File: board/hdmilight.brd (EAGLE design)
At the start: 68.5 x 68.6 mm, 72 parts, among them IC1 REG1117, IC2 REG1117, Q1 28.6363MHz

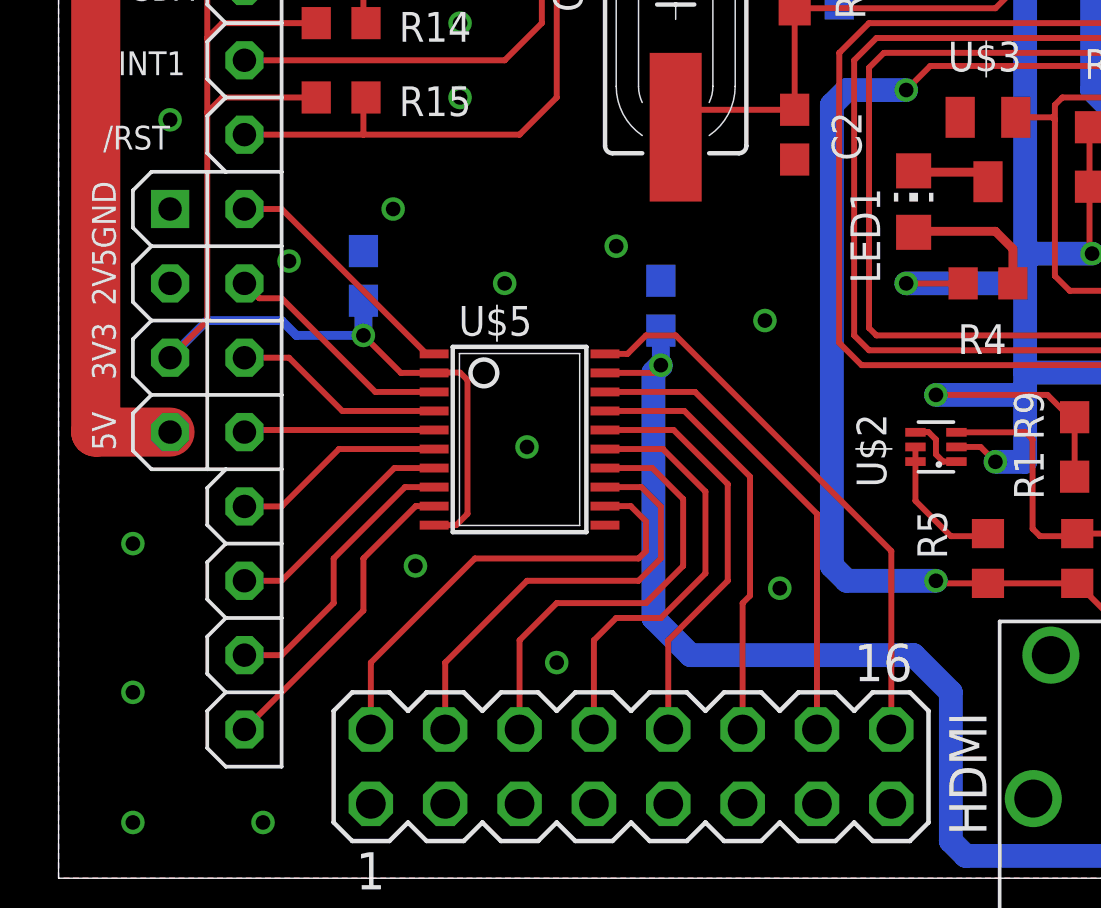
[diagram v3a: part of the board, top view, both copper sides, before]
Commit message: receiver board: replaced TXB0108 level shifter with a 74HCT541
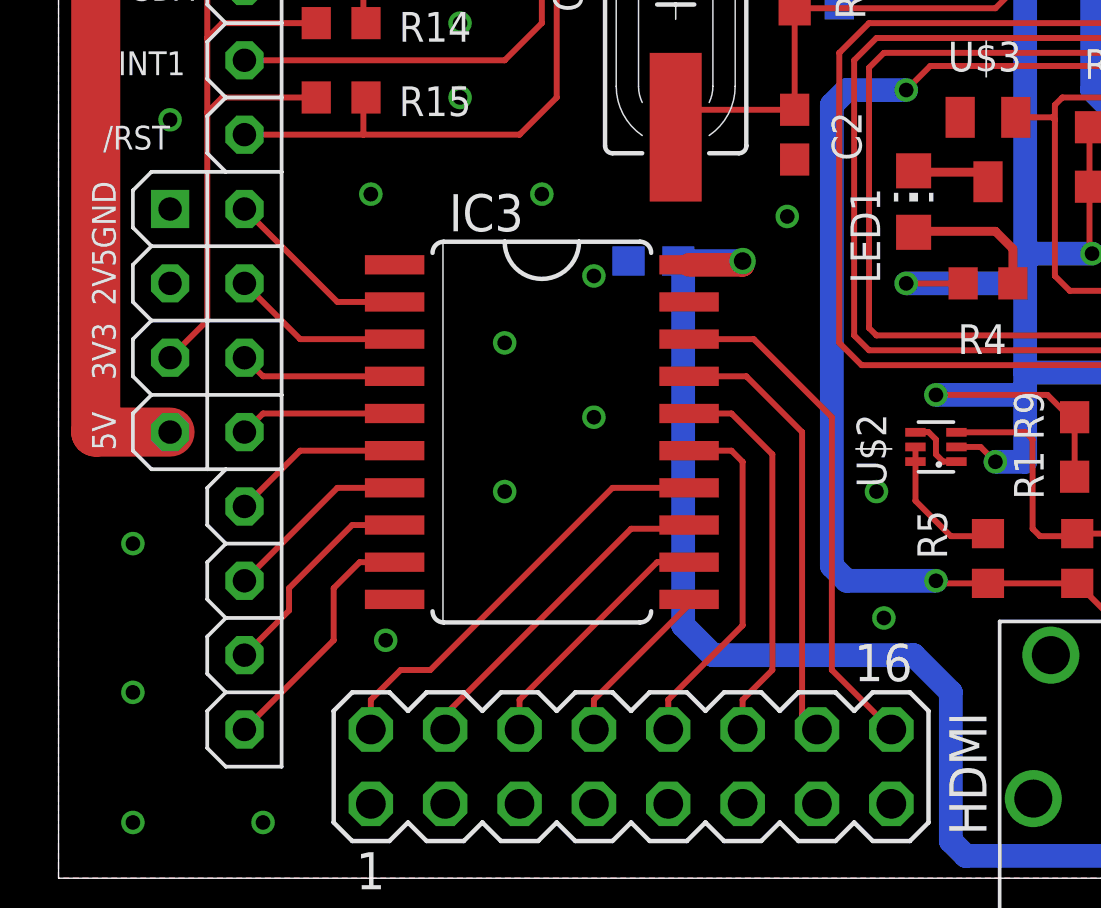
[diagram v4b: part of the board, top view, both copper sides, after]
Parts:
- removed C20: 0.1uF, resistor:C0603
- removed U$5: TXB0108, __SR:TSSOP20
- added IC3: 74HCT541DW, 74xx-eu:SO20W
- moved C21 1.55 mm to (20.3, 21.1), turned to 0 degrees
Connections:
- removed net N$46: SV1.10, U$5.16
- removed net N$47: SV1.8, U$5.15
- removed net N$48: SV1.6, U$5.14
- removed net N$49: SV1.4, U$5.13
- removed net N$50: U$5.1, U$7.A41
- removed net N$51: SV1.16, U$5.20
- new net N$10: IC3.8, U$7.A47
- new net N$11: IC3.7, U$7.A46
- new net N$12: IC3.6, U$7.A45
- new net N$17: IC3.5, U$7.A44
- new net N$42: IC3.16, SV1.12
- new net N$9: IC3.9, U$7.A48
- net +3V3: no longer C20.1, U$5.10, U$5.2
- net GND: now also IC3.1, IC3.10, IC3.19; no longer C20.2, U$5.11
- net N$18: now also IC3.4, U$7.A43; no longer SV1.2, U$5.12
- net N$35: now also IC3.3, U$7.A42; no longer U$5.9, U$7.A48
- net N$36: now also IC3.2, U$7.A41; no longer U$5.8, U$7.A47
- net N$37: now also IC3.14, SV1.2; no longer U$5.7, U$7.A46
- net N$38: now also IC3.11, SV1.8; no longer U$5.6, U$7.A45
- net N$39: now also IC3.12, SV1.6; no longer U$5.5, U$7.A44
- net N$40: now also IC3.13, SV1.4; no longer U$5.4, U$7.A43
- net N$41: now also IC3.15, SV1.10; no longer U$5.3, U$7.A42
- net N$44: now also IC3.17; no longer U$5.18
- net N$45: now also IC3.18, SV1.16; no longer SV1.12, U$5.17
- net VCC_5V0: now also IC3.20; no longer U$5.19
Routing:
- net N$51: track 19.2 -> 0.00 mm
- net +3V3: track 44.4 -> 25.8 mm, vias 1 -> 0
- net N$49: track 15.1 -> 0.00 mm
- net N$48: track 15.1 -> 0.00 mm
- net N$47: track 14.6 -> 0.00 mm
- net N$46: track 14.2 -> 0.00 mm
- net N$42: track 0.00 -> 13.2 mm
- net N$18: track 15.9 -> 5.39 mm
- net N$9: track 0.00 -> 8.54 mm
- net N$50: track 8.53 -> 0.00 mm
- net N$10: track 0.00 -> 7.42 mm
- net N$37: track 8.08 -> 14.9 mm
- net N$11: track 0.00 -> 6.45 mm
- net N$12: track 0.00 -> 5.92 mm
- net N$17: track 0.00 -> 5.39 mm
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
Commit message: receiver board: changed value of IP4776CZ38 ESD protection IC to TPD12S520
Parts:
- U$4: value IP4776CZ38 -> TPD12S520
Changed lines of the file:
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@@
 </element>
 <element name="U$1" library="__SR" package="FCI_HDMI_SOCKET_10029449-001RCF" value="FCI_HDMI_SOCKET_10029449-001RCF" x="41.148" y="7.62"/>
-<element name="U$4" library="__SR" package="TSSOP38" value="IP4776CZ38" x="42.926" y="17.272" rot="R180"/>
+<element name="U$4" library="__SR" package="TSSOP38" value="TPD12S520" x="42.926" y="17.272" rot="R180"/>
 <element name="F1" library="SparkFun" package="PTC-1206" value="1206L050YR" x="21.59" y="62.23" smashed="yes" rot="R90">
 <attribute name="NAME" x="22.606" y="66.04" size="1.016" layer="25" rot="R180"/>

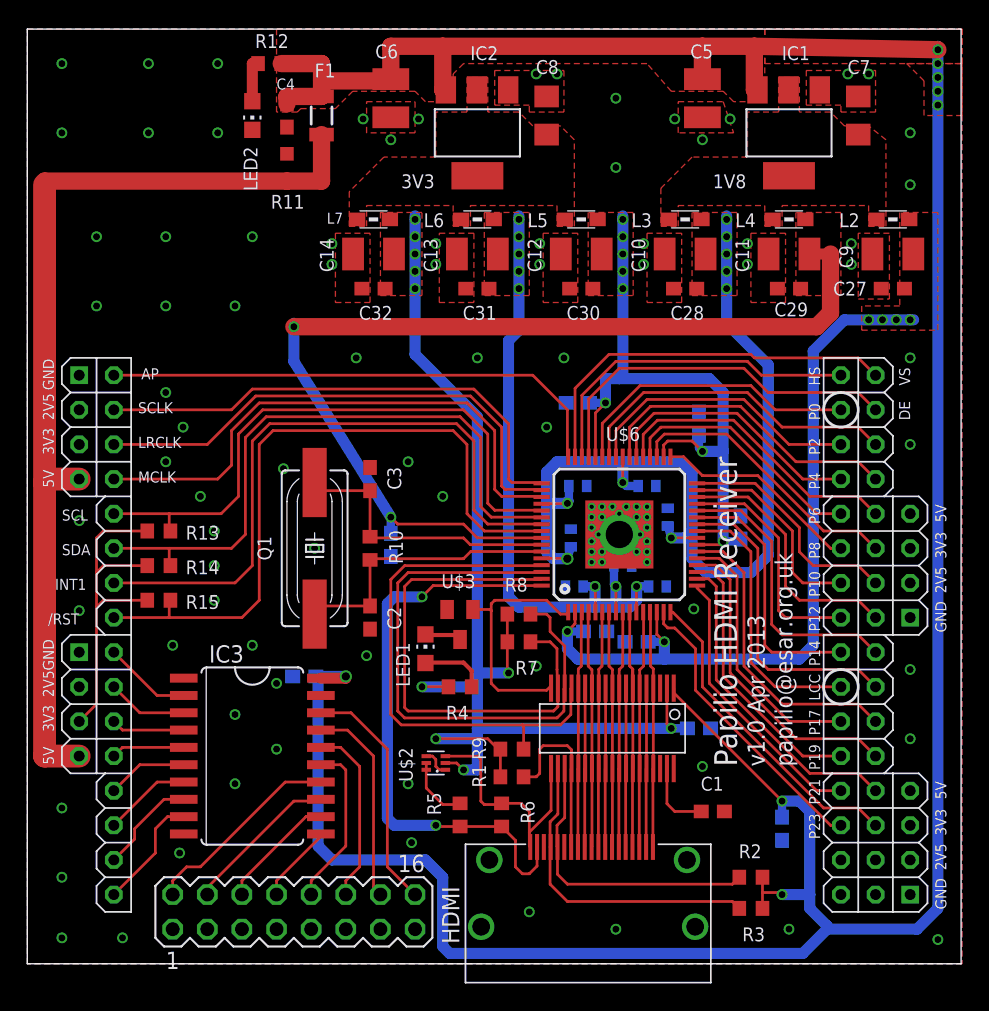
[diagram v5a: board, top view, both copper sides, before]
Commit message: receiver board: merged changes from Jet:
 * added "power" and "hotplug" LED labels
 * added LED polarity symbols
 * moved C7/C8 labels off of vias
 * moved vias from under SCL and RST labels
 * moved vias from under R13/14/15 labels
 * added + symbols on polarised caps C7-14
 * added R16: 10K between VCC_3V3 and TPD12S520 LV_SUPPLY
 * increased drill size for ADV7611 ground pad from 12mil to 13mil
 * fixed schematic net labels

also changed:

 * edited pin header package to remove the "1" and "16" labels
 * added channel number labels to output channel header
 * changed all text to same vector font
 * added OSHW logo
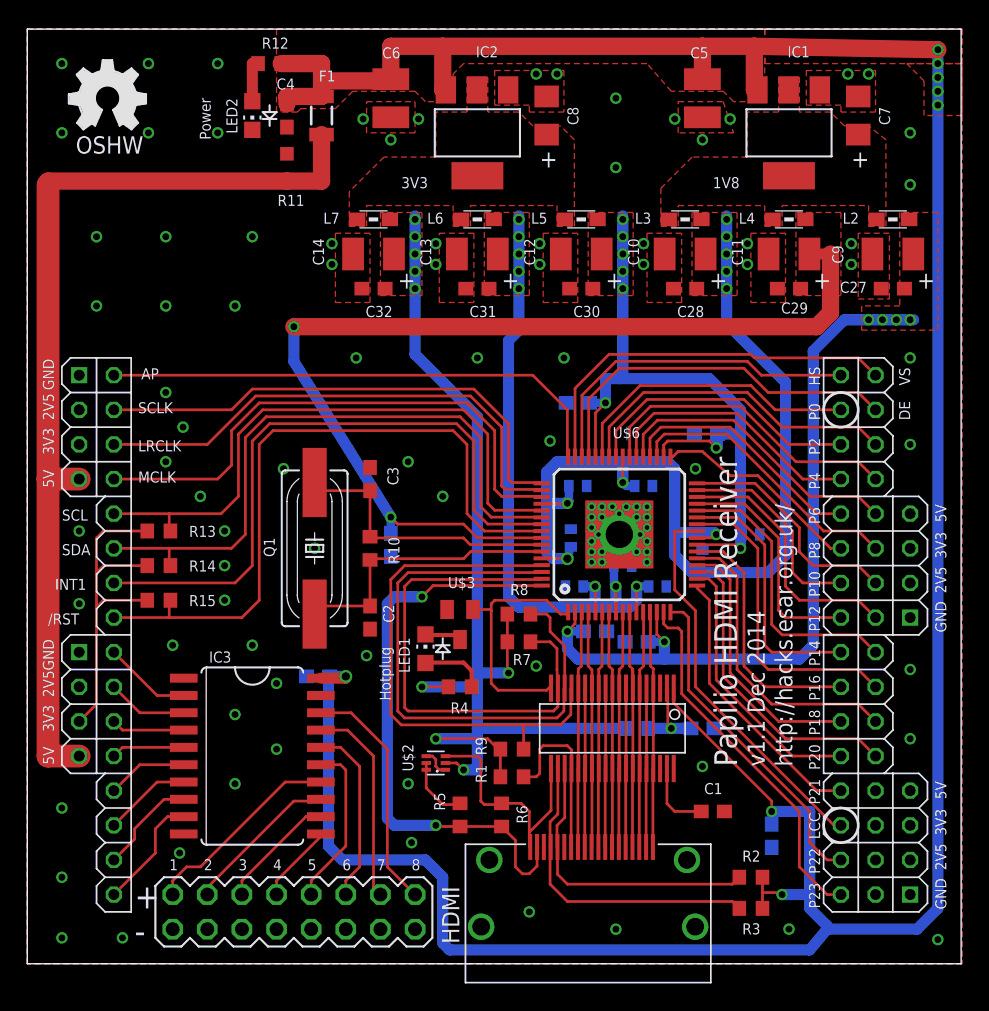
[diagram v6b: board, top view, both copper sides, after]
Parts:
- added LOGO1: OSHW_LOGO_FILLX0200-NT, ohw-logo:OSHW_FILLX200_NOTEXT
- added R16: 10K, resistor:R0603
- C35: device resistor:C0603 -> resistor:C0402
- moved C23 3.10 mm to (49.5, 31.0), turned to 270 degrees
- moved C21 1.02 mm to (21.3, 21.1)
- moved C26 0.92 mm to (54.6, 9.40)
- moved C35 0.92 mm to (53.1, 31.5), turned to 180 degrees
- moved C24 0.92 mm to (49.8, 38.9), turned to 0 degrees
- moved C15 0.25 mm to (45.2, 35.1)
- moved C19 0.25 mm to (49.5, 17.3)
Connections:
- new net N$47: C19.1, R16.2, U$4.P$2
- net LLC: now also U$7.A30; no longer U$7.A26
- net P16: now also U$7.A26; no longer U$7.B27
- net P17: now also U$7.B27; no longer U$7.A27
- net P18: now also U$7.A27; no longer U$7.B28
- net P19: now also U$7.B28; no longer U$7.A28
- net P20: now also U$7.A28; no longer U$7.B29
- net P22: now also U$7.A31; no longer U$7.B30
- net P23: now also U$7.A32; no longer U$7.A30
- net VCC_3V3: now also R16.1; no longer C19.1, U$4.P$2
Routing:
- net LLC: track 20.1 -> 28.6 mm
- net VCC_3V3: track 86.6 -> 78.9 mm, vias 10 -> 9
- net N$47: track 0.00 -> 6.25 mm, vias 0 -> 1
- net P23: track 21.8 -> 27.1 mm
- net P20: track 23.6 -> 20.0 mm
- net P18: track 22.9 -> 19.3 mm
- net P16: track 22.3 -> 18.7 mm
- net P19: track 20.2 -> 22.7 mm
- net P17: track 19.5 -> 22.1 mm
- net DVDD_1V8: track 75.1 -> 76.8 mm
- net DVDDIO_3V3: track 49.7 -> 51.4 mm
- net VCC_5V0: track 228.6 -> 227.2 mm
- net P22: track 23.5 -> 24.5 mm
- net +5V: track 71.1 -> 70.2 mm
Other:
- board text added: "*** THIS REVISION HAS NOT BEEN TESTED ***"
- board text added: "+"
- board text added: "-"
- board text added: "1"
- board text added: "2"
- board text added: "3"
- board text added: "4"
- board text added: "5"
- board text added: "6"
- board text added: "7"
- board text added: "8"
- board text added: "Hotplug"
- board text added: "OSHW"
- board text added: "P16"
- board text added: "P18"
- board text added: "P20"
- board text added: "P22"
- board text added: "Power"
- board text added: "http://hacks.esar.org.uk/"
- board text added: "v1.1 Dec 2014"
- board text removed: "P17"
- board text removed: "P19"
- board text removed: "papilio@esar.org.uk"
- board text removed: "v1.0 Apr 2013"
